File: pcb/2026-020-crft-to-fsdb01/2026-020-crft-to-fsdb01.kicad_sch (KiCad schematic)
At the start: 0 parts

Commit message: Generate rev. 1 of schematic
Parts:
- added C1: 10u, Capacitor_SMD:C_0603_1608Metric, symbol Device:C
- added C10, C2, C5, C6, C7, C8: 100n, Capacitor_SMD:C_0603_1608Metric, symbol Device:C
- added C3, C4: 1u, Capacitor_SMD:C_0603_1608Metric, symbol Device:C
- added C9: 4.7u, Capacitor_SMD:C_0603_1608Metric, symbol Device:C
- added D1, D2: B5819W, Diode_SMD:D_SOD-123, symbol Device:D_Schottky
- added D3: KP-1608QBC-D, LED_SMD:LED_0603_1608Metric, symbol Device:LED
- added D4: ASMT-RF45-AN002, LED_SMD:LED_0603_1608Metric, symbol Device:LED
- added J1: CRSF_IN, Connector_PinHeader_2.54mm:PinHeader_1x03_P2.54mm_Vertical, symbol Connector_Generic:Conn_01x03
- added J2: FSDB01_OUT, Connector_PinHeader_2.54mm:PinHeader_1x03_P2.54mm_Vertical, symbol Connector_Generic:Conn_01x03
- added J3: USB-C, Connector_USB:USB_C_Receptacle_HRO_TYPE-C-31-M-12, symbol Connector:USB_C_Receptacle_USB2.0_16P
- added J4: SWD, Connector_Molex:Molex_PicoBlade_53261-0571_1x05-1MP_P1.25mm_Horizontal, symbol Connector_Generic_MountingPin:Conn_01x05_MountingPin
- added R1, R5: 100k, Resistor_SMD:R_0603_1608Metric, symbol Device:R
- added R2, R6: 33k, Resistor_SMD:R_0603_1608Metric, symbol Device:R
- added R3, R4: 5.1k, Resistor_SMD:R_0603_1608Metric, symbol Device:R
- added R7: 10, Resistor_SMD:R_0603_1608Metric, symbol Device:R
- added R8: 91, Resistor_SMD:R_0603_1608Metric, symbol Device:R
- added U1: STM32G0B1CET6, Package_QFP:LQFP-48_7x7mm_P0.5mm, symbol MCU_ST_STM32G0:STM32G0B1CETx
- added U2: NCP551SN33T1G, Package_TO_SOT_SMD:SOT-23-5, symbol crsf_fsdb01:NCP551SN33T1G
- added U3: USBLC6-2SC6, Package_TO_SOT_SMD:SOT-23-6, symbol Power_Protection:USBLC6-2SC6
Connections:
- new net: C3.1, D1.1 (K), D2.1 (K), U2.1 (VIN), U2.3 (EN)
- new net: D4.2 (A), R8.2
- new net: D3.2 (A), R7.2
- new net +3V3: C4.1, C6.1, C7.1, C8.1, C9.1, J4.1 (Pin_1), R7.1, R8.1, U1.4 (VBAT), U1.5 (VREF+), U1.6 (VDD), U2.5 (VOUT)
- new net CC1: J3.A5 (CC1), R3.1
- new net CC2: J3.B5 (CC2), R4.1
- new net CRSF: J1.1 (Pin_1), U1.46 (PB7)
- new net FSDB01: J2.1 (Pin_1), U1.28 (PA8)
- new net GND: C1.2, C10.2, C2.2, C3.2, C4.2, C5.2, C6.2, C7.2, C8.2, C9.2, J1.3 (Pin_3), J2.3 (Pin_3), J3.A1 (GND), J3.A12 (GND), J3.B1 (GND), J3.B12 (GND), J3.SH (SHIELD), J4.5 (Pin_5), R2.2, R3.2, R4.2, R6.2, U1.7 (VSS), U2.2 (GND), U3.2 (GND)
- new net LED_BLUE: D3.1 (K), U1.19 (PB0)
- new net LED_RED: D4.1 (K), U1.20 (PB1)
- new net NRST: C10.1, J4.4 (Pin_4), U1.10 (PF2)
- new net SWCLK: J4.3 (Pin_3), U1.36 (PA14)
- new net SWDIO: J4.2 (Pin_2), U1.35 (PA13)
- new net USB_DM: J3.A7 (D-), J3.B7 (D-), U3.1 (I/O1)
- new net USB_DM_MCU: U1.33 (PA9/PA11), U3.6 (I/O1)
- new net USB_DP: J3.A6 (D+), J3.B6 (D+), U3.3 (I/O2)
- new net USB_DP_MCU: U1.34 (PA10/PA12), U3.4 (I/O2)
- new net VBUS: D2.2 (A), J3.A4 (VBUS), J3.A9 (VBUS), J3.B4 (VBUS), J3.B9 (VBUS), R5.1, U3.5 (VBUS)
- new net VBUS_SENSE: C5.1, R5.2, R6.1, U1.12 (PA1)
- new net VIN: C1.1, D1.2 (A), J1.2 (Pin_2), J2.2 (Pin_2), R1.1
- new net VIN_SENSE: C2.1, R1.2, R2.1, U1.11 (PA0)
- no-connect marks 0 -> 36

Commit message: Update C1
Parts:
- C1: value 10u -> 10u 16V; footprint Capacitor_SMD:C_0603_1608Metric -> Capacitor_Tantalum_SMD:CP_EIA-3528-21_Kemet-B; symbol Device:C -> Device:C_Polarized; MPN (none) -> TAJB106M016RNJ; Manufacturer (none) -> KYOCERA AVX
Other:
- title: (none) -> #2026-020 CRSF-to-FSDB01
- moved on the sheet: C2, J1, J2, R1, R2

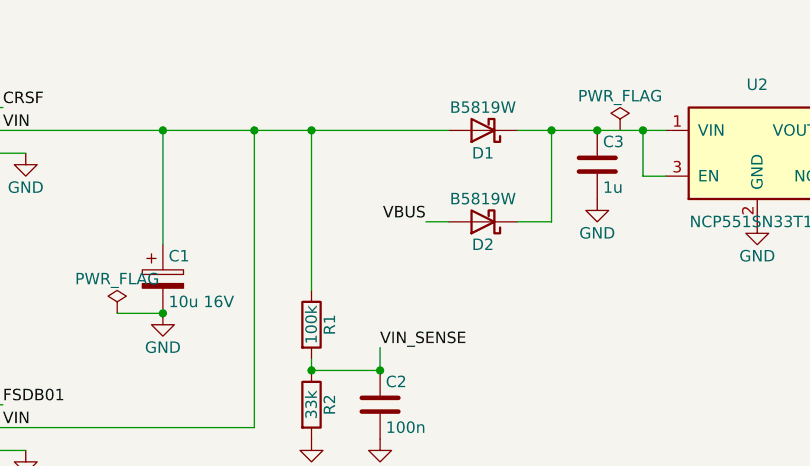
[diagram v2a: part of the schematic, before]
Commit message: Update parts, export BOM to Google Sheet
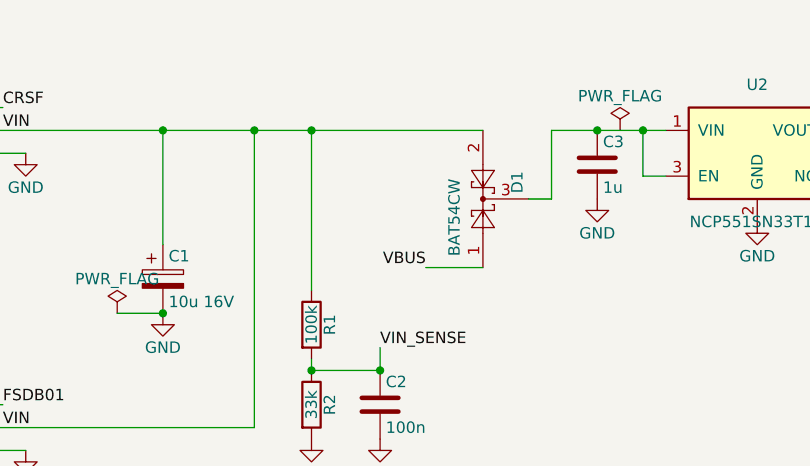
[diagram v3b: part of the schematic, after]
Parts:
- removed D1, D2: B5819W, Diode_SMD:D_SOD-123, symbol Device:D_Schottky
- added D1: BAT54CW, Package_TO_SOT_SMD:SOT-323_SC-70, symbol Diode:BAT54CW
- J3: footprint Connector_USB:USB_C_Receptacle_HRO_TYPE-C-31-M-12 -> Connector_USB:USB_C_Receptacle_GCT_USB4105-xx-A_16P_TopMnt_Horizontal; MPN (none) -> USB4105-GF-A-120; Manufacturer (none) -> GCT
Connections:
- net VBUS: now also D1.1
- net VIN: now also D1.2
- net at C3.1, U2.1 (VIN), U2.3 (EN): now also D1.3

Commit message: Renumber diodes
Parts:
- renumbered D3 to D2, D4 to D3
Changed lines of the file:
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@@
 		(on_board yes)
 		(dnp no)
-		(property "Reference" "D4"
+		(property "Reference" "D3"
 			(at 243.84 114.3 0)
 			(show_name no)
@@
 			(project "2026-020-crft-to-fsdb01"
 				(path "/61016c77-80a0-4d46-8842-2d3ef9287067"
-					(reference "D4")
+					(reference "D3")
 					(unit 1)
 				)
@@
 		(on_board yes)
 		(dnp no)
-		(property "Reference" "D3"
+		(property "Reference" "D2"
 			(at 231.14 114.3 0)
 			(show_name no)
@@
 			(project "2026-020-crft-to-fsdb01"
 				(path "/61016c77-80a0-4d46-8842-2d3ef9287067"
-					(reference "D3")
-					(unit 1)
-				)
+					(reference "D2")
+					(unit 1)
+				)
